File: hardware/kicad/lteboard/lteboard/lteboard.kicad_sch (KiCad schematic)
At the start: 0 parts

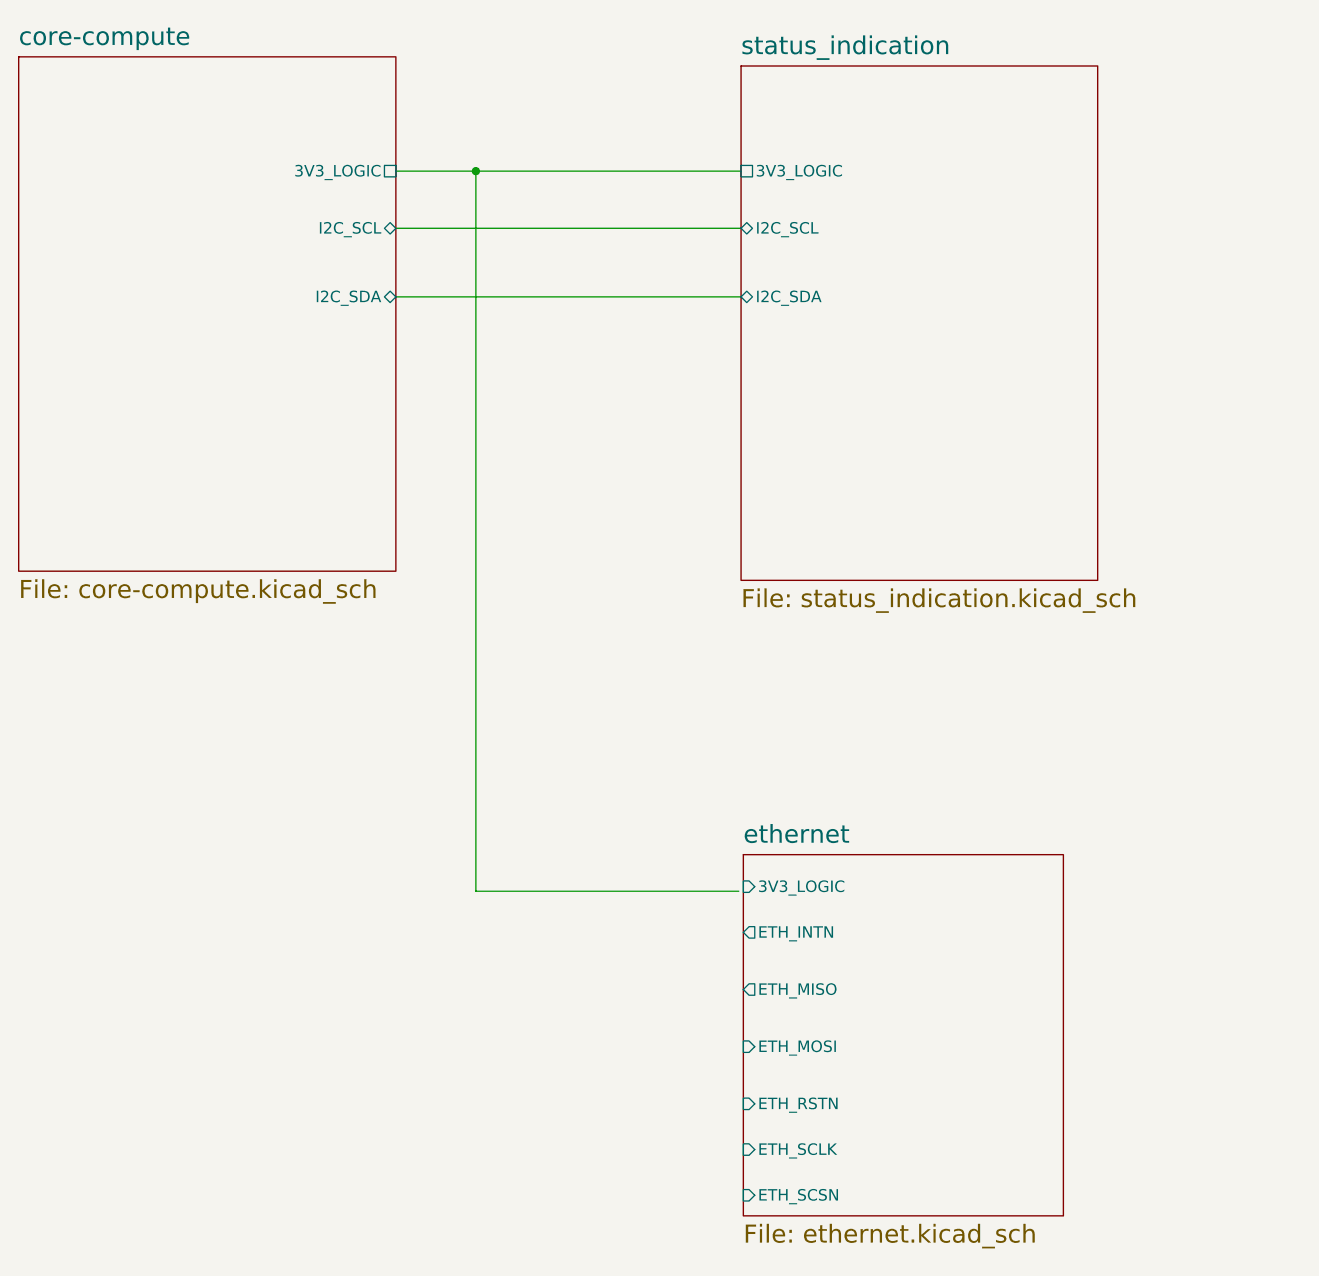
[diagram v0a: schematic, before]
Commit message: Complete LTE subsystem: schematic capture, master-sheet integration, and the VBAT_LTE rail fix
- lte.kicad_sch: modem (EG915UEUAC-N05-SNNSA), TXB0102 UART level shifter, pre-biased
  transistor PWRKEY/RESET_N drive (Q4/Q5), SIM interface + ESD protection (D1, now with
  all 4 channels wired including the SIM VDD line), antenna matching network, VBAT
  decoupling. Two schematic-level gaps found while verifying the master-sheet integration
  (D1's unwired 4th ESD channel, two missing No-Connect flags on U4) are fixed and
  re-verified against a fresh netlist reconstruction.
- lteboard.kicad_sch: LTE sheet symbol + its 6 hierarchical pins added and checked
  pin-for-pin against lte.kicad_sch's own hierarchical labels (name + direction) - exact
  match. Not yet wired into the rest of the board; that needs roadmap steps 6 (pin
  planning) and 7 (board-to-board connector), neither started.
- Carries the VBAT_LTE rail fix from 2026-09-13 that had never been committed: renamed
  from 3V3_LTE and retapped (137k -> 115k) from ~3.3V (the exact floor of Quectel's spec,
  zero margin) to ~3.82V, matching Quectel's typical - power.md, architecture.md,
  analog-io.md, and the corresponding ioboard.kicad_sch/power.kicad_sch label+value
  changes.
- Also includes an RS485_RXD/RS485_TXD pin/direction correction on ioboard.kicad_sch's
  root sheet pins, and RS232/ioboard reference-designator re-annotation (RS232's parts
  renumbered to fit the whole-board sequence), both already sitting in the working tree.
- Docs: lte.md (full build plan through Step 7), lte_bom.csv, README.md's new LTE section,
  roadmap.md's LTE line updated from "plan drafted" to done through schematic capture/BOM.
- Removed 4 stale duplicate doc files (CLAUDE-1.md, roadmap-1.md, ethernet-1.md,
  README-1.md), confirmed byte-identical to their real counterparts before deletion.

Co-Authored-By: Claude Sonnet 5 <noreply@anthropic.com>
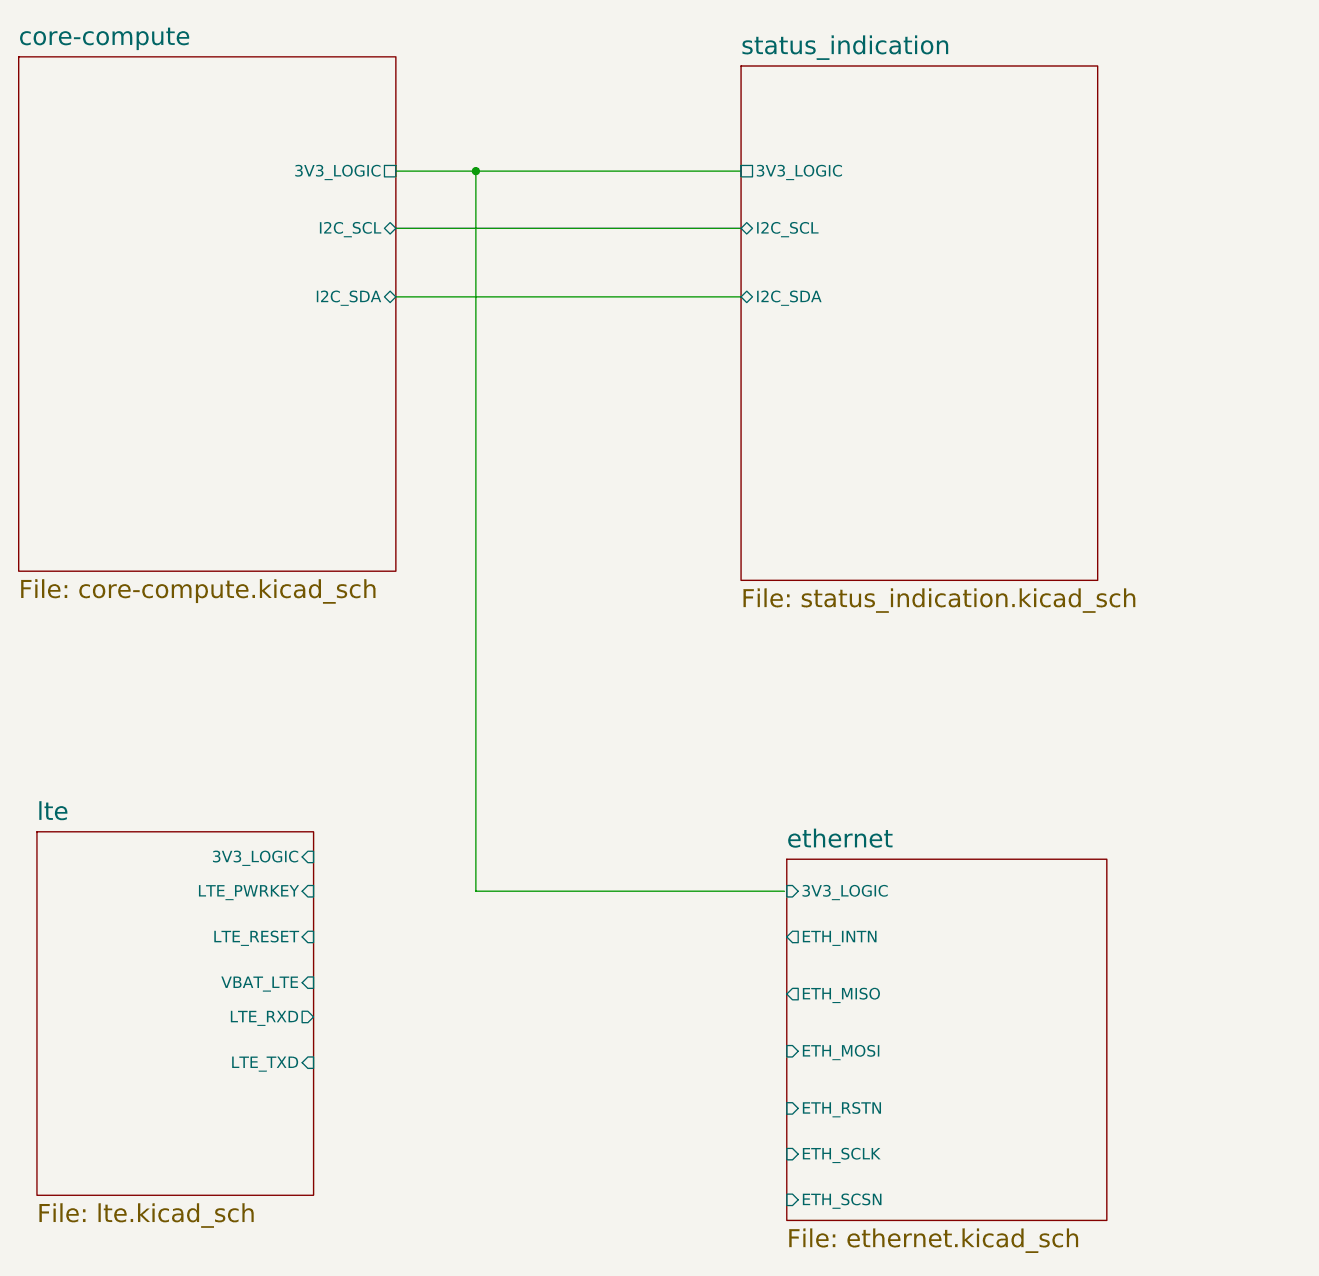
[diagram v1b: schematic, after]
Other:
- added sheet lte (lte.kicad_sch)
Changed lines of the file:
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@@
 	(wire
 		(pts
-			(xy 115.57 130.81) (xy 86.36 130.81)
+			(xy 86.36 130.81) (xy 120.65 130.81)
 		)
 		(stroke
@@
 	)
 	(sheet
-		(at 116.078 126.746)
+		(at 37.592 124.206)
+		(size 30.734 40.386)
+		(exclude_from_sim no)
+		(in_bom yes)
+		(on_board yes)
+		(dnp no)
+		(fields_autoplaced yes)
+		(stroke
+			(width 0.1524)
+			(type solid)
+		)
+		(fill
+			(color 0 0 0 0.0000)
+		)
+		(property "Sheetname" "lte"
+			(at 37.592 123.1294 0)
+			(effects
+				(font
+					(size 2 2)
+				)
+				(justify left bottom)
+			)
+		)
+		(property "Sheetfile" "lte.kicad_sch"
+			(at 37.592 165.4686 0)
+			(effects
+				(font
+					(size 2 2)
+				)
+				(justify left top)
+			)
+		)
+		(pin "3V3_LOGIC" input
+			(at 68.326 127 0)
+			(effects
+				(font
+					(size 1.27 1.27)
+				)
+				(justify right)
+			)
+		)
+		(pin "LTE_PWRKEY" input
+			(at 68.326 130.81 0)
+			(effects
+				(font
+					(size 1.27 1.27)
+				)
+				(justify right)
+			)
+		)
+		(pin "LTE_RESET" input
+			(at 68.326 135.89 0)
+			(effects
+				(font
+					(size 1.27 1.27)
+				)
+				(justify right)
+			)
+		)
+		(pin "VBAT_LTE" input
+			(at 68.326 140.97 0)
+			(effects
+				(font
+					(size 1.27 1.27)
+				)
+				(justify right)
+			)
+		)
+		(pin "LTE_RXD" output
+			(at 68.326 144.78 0)
+			(effects
+				(font
+					(size 1.27 1.27)
+				)
+				(justify right)
+			)
+		)
+		(pin "LTE_TXD" input
+			(at 68.326 149.86 0)
+			(effects
+				(font
+					(size 1.27 1.27)
+				)
+				(justify right)
+			)
+		)
+		(instances
+			(project "lteboard"
+				(path "/e3cbe890-827c-4e3e-bf4e-d33595c4d0b3"
+					(page "5")
+				)
+			)
+		)
+	)
+	(sheet
+		(at 120.904 127.254)
 		(size 35.56 40.132)
 		(exclude_from_sim no)
@@
 		)
 		(property "Sheetname" "ethernet"
-			(at 116.078 125.6694 0)
+			(at 120.904 126.1774 0)
 			(effects
 				(font
@@
 		)
 		(property "Sheetfile" "ethernet.kicad_sch"
-			(at 116.078 167.7546 0)
+			(at 120.904 168.2626 0)
 			(effects
 				(font
@@
 		)
 		(pin "3V3_LOGIC" input
-			(at 116.078 130.302 180)
+			(at 120.904 130.81 180)
 			(effects
 				(font
@@
 		)
 		(pin "ETH_INTN" output
-			(at 116.078 135.382 180)
+			(at 120.904 135.89 180)
 			(effects
 				(font
@@
 		)
 		(pin "ETH_MISO" output
-			(at 116.078 141.732 180)
+			(at 120.904 142.24 180)
 			(effects
 				(font
@@
 		)
 		(pin "ETH_MOSI" input
-			(at 116.078 148.082 180)
+			(at 120.904 148.59 180)
 			(effects
 				(font
@@
 		)
 		(pin "ETH_RSTN" input
-			(at 116.078 154.432 180)
+			(at 120.904 154.94 180)
 			(effects
 				(font
@@
 		)
 		(pin "ETH_SCLK" input
-			(at 116.078 159.512 180)
+			(at 120.904 160.02 180)
 			(effects
 				(font
@@
 		)
 		(pin "ETH_SCSN" input
-			(at 116.078 164.592 180)
-			(effects
-				(font
+			(at 120.904 165.1 180)
+			(effects
+				(font
